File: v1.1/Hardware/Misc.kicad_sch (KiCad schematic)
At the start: 10 parts, among them J4 FAN, J6 Conn_01x04, U16 ADuM1201AR

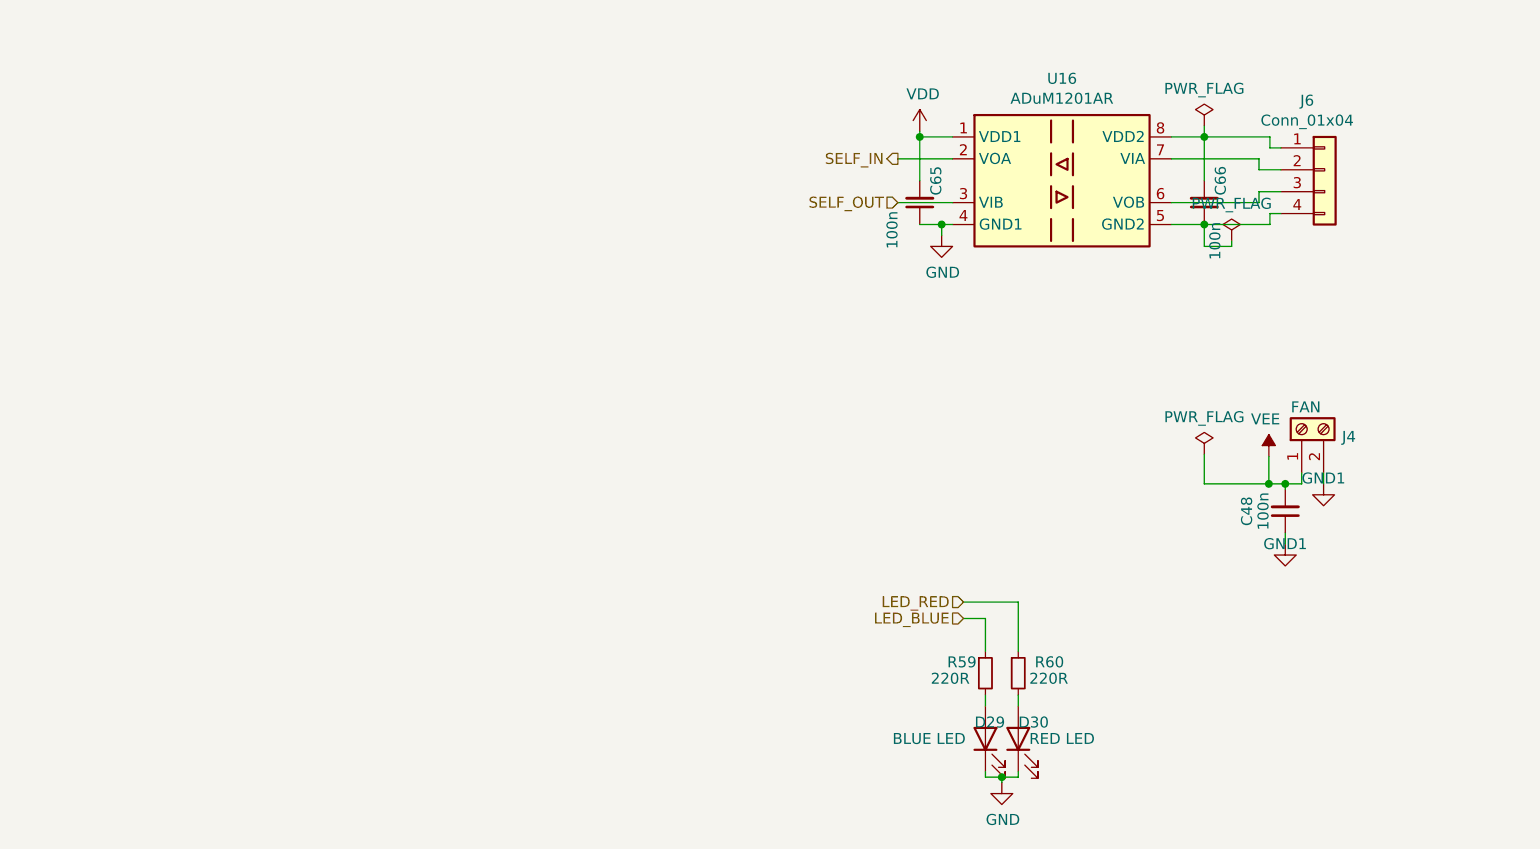
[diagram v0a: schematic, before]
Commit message: v1.1&v1.2 PCB addition.
#####v1.1#####
+Change of MCU; STM32F334C8T6 instead of STM32F103C8T6.
+Filtering 3rd order components of the square wave.
+Use  4 capacitors.
+Adapted to generic transformer(primary 6.4mH, secondary 14.4mH)
+Faster IGBT.

########v1.2#######
+Measures only PZT current and voltage.
+Differential inputs.
+Analog circuitry is capable of measuring four quadrant voltage, current and complex impedance.
+Half bridge configuration.
+Gate resistance of the IGBT's lowered.
+Only USART based touch panel can be connected; not conventional LCD.
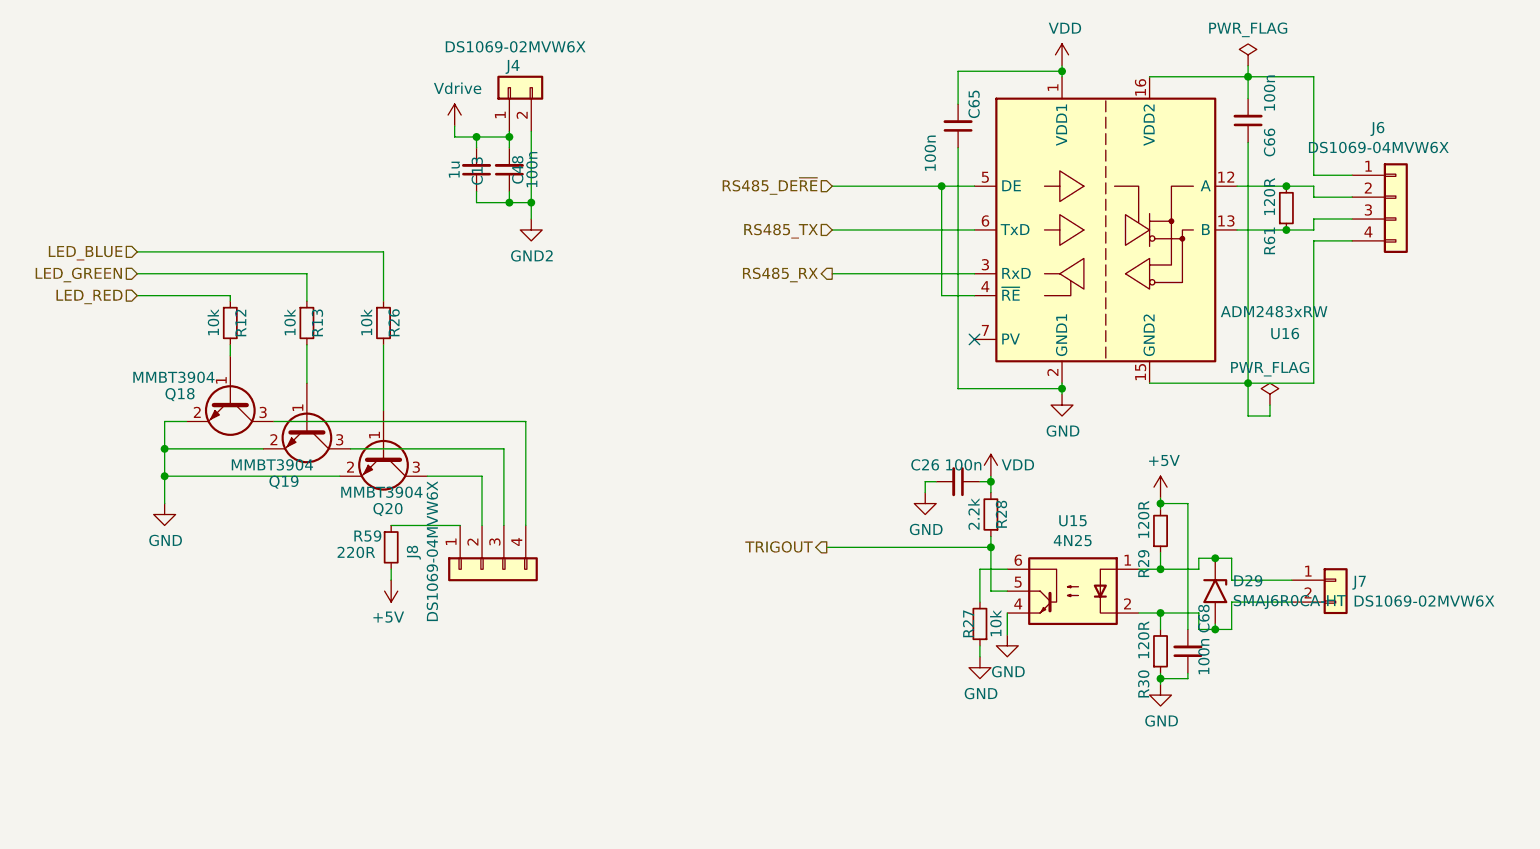
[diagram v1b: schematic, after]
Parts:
- removed D29: BLUE LED, LED_SMD:LED_0805_2012Metric_Pad1.15x1.40mm_HandSolder, symbol Device:LED
- removed D30: RED LED, LED_SMD:LED_0805_2012Metric_Pad1.15x1.40mm_HandSolder, symbol Device:LED
- removed J4: FAN, oe_connector:DG128-5.0-02P-14-00AH, symbol Connector:Screw_Terminal_01x02
- removed R60: 220R, Resistor_SMD:R_0805_2012Metric_Pad1.15x1.40mm_HandSolder, symbol Device:R_Small
- removed U16: ADuM1201AR, Package_SO:SOIC-8_3.9x4.9mm_P1.27mm, symbol Isolator:ADuM1201AR
- added C13: 1u, Capacitor_SMD:C_0805_2012Metric, symbol Device:C_Small
- added C26, C68: 100n, Capacitor_SMD:C_0805_2012Metric, symbol Device:C_Small
- added D29: SMAJ6R0CA-HT, oe_diode:DO214AC_SMA, symbol Diode:1.5KExxA
- added J4, J7: DS1069-02MVW6X, Connector_JST:JST_EH_B2B-EH-A_1x02_P2.50mm_Vertical, symbol Connector_Generic:Conn_01x02
- added J8: DS1069-04MVW6X, Connector_JST:JST_EH_B4B-EH-A_1x04_P2.50mm_Vertical, symbol Connector_Generic:Conn_01x04
- added Q18, Q19, Q20: MMBT3904, Package_TO_SOT_SMD:SOT-23, symbol Transistor_BJT:MMBT3904
- added R12, R13, R26, R27: 10k, Resistor_SMD:R_0805_2012Metric, symbol Device:R_Small
- added R28: 2.2k, Resistor_SMD:R_0805_2012Metric, symbol Device:R_Small
- added R29, R30, R61: 120R, Resistor_SMD:R_0805_2012Metric, symbol Device:R_Small
- added U15: 4N25, Package_DIP:DIP-6_W7.62mm, symbol Isolator:4N25
- added U16: ADM2483xRW, Package_SO:SOIC-16W_7.5x10.3mm_P1.27mm, symbol Interface_UART:ADM2483xRW
- C48: footprint Capacitor_THT:C_Rect_L7.2mm_W2.5mm_P5.00mm_FKS2_FKP2_MKS2_MKP2 -> Capacitor_SMD:C_0805_2012Metric; Link https://ozdisan.com/passive-components/capacitors/film-capa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 -> https://ozdisan.com/passive-components/capacitors/smt-smd-a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; Price 0.28918TL -> 0.10509TL
- C65, C66: footprint Capacitor_SMD:C_0805_2012Metric_Pad1.15x1.40mm_HandSolder -> Capacitor_SMD:C_0805_2012Metric
- J6: value Conn_01x04 -> DS1069-04MVW6X; footprint Connector_PinHeader_2.54mm:PinHeader_1x04_P2.54mm_Vertical -> Connector_JST:JST_EH_B4B-EH-A_1x04_P2.50mm_Vertical; Link https://ozdisan.com/connectors-and-interconnects/headers/pi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 -> https://ozdisan.com/Product/Detail/347998/DS1069-04MVW6X; Price 0.0885TL -> 0.08950TL
- R59: footprint Resistor_SMD:R_0805_2012Metric_Pad1.15x1.40mm_HandSolder -> Resistor_SMD:R_0805_2012Metric
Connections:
- net GND: now also C26.2, C68.1, Q18.2 (E), Q19.2 (E), Q20.2 (E), R27.1, R30.1, U15.4, U16.2 (GND1), U16.8 (GND1)
- net LED_BLUE: now also R26.1; no longer R59.1
- net LED_RED: now also R12.1
- net VDD: now also C26.1, R28.2, U16.1 (VDD1)
- net +5V: now reaches R59.2
- net +5V: now also C68.2, R29.2
- net at C66.1, J6.4 (Pin_4): now also U16.15 (GND2), U16.9 (GND2)
- net at C66.2, J6.1 (Pin_1): now also U16.16 (VDD2)
- net at J6.2 (Pin_2): now also R61.2, U16.12 (A)
- net at J6.3 (Pin_3): now also R61.1, U16.13 (B)
- net GND1 renamed GND2
- net GND2: now also C13.1, J4.2 (Pin_2)
- net VEE renamed Vdrive
- net Vdrive: now also C13.2, J4.1 (Pin_1)
- new net: Q18.1 (B), R12.2
- new net: J8.4 (Pin_4), Q18.3 (C)
- new net: J8.1 (Pin_1), R59.1
- new net: J8.2 (Pin_2), Q20.3 (C)
- new net: J8.3 (Pin_3), Q19.3 (C)
- new net: Q19.1 (B), R13.2
- new net: Q20.1 (B), R26.2
- new net: D29.1 (A1), J7.1 (Pin_1), R29.1, U15.1
- new net: D29.2 (A2), J7.2 (Pin_2), R30.2, U15.2
- new net: R27.2, U15.6
- new net LED_GREEN: R13.1
- new net RS485_DE~RE: U16.4 (~RE), U16.5 (DE)
- new net RS485_RX: U16.3 (RxD)
- new net RS485_TX: U16.6 (TxD)
- new net TRIGOUT: R28.1, U15.5
- no-connect marks 0 -> 1
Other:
- moved on the sheet: C65, C66, J6, R59
